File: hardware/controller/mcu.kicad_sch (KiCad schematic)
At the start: 21 parts, among them J12 USB_C_Receptacle_USB2.0_14P, J5 Screw_Terminal_01x02, J6 Screw_Terminal_01x02, U1 ESP32-C3-MINI-1, U6 TPS1H200AQDGNRQ1

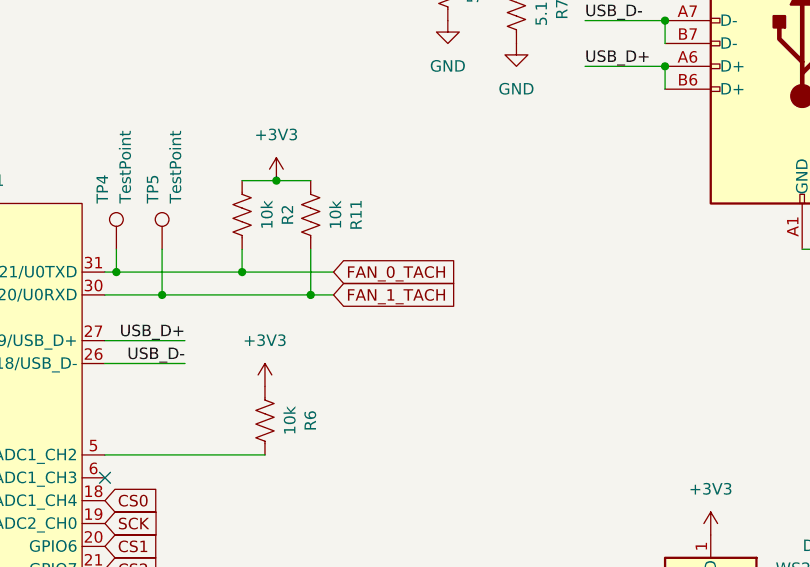
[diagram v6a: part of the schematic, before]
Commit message: Rounded corners, fixed up labels
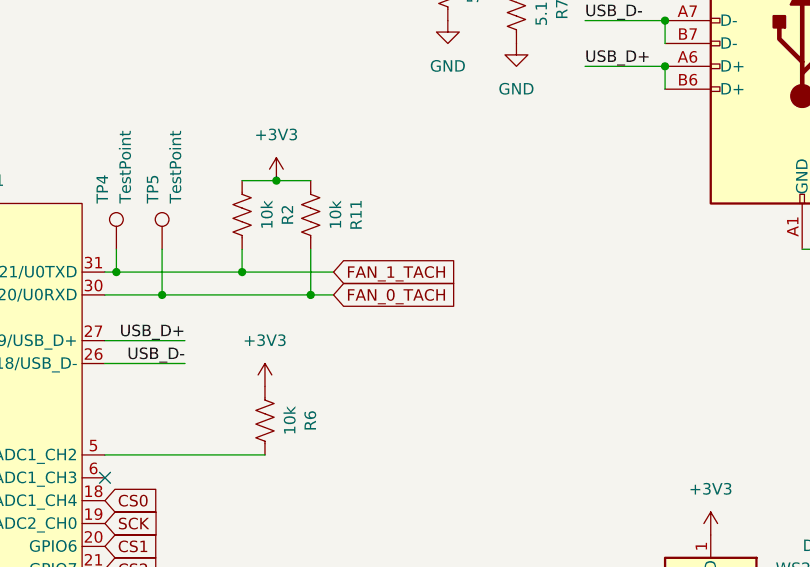
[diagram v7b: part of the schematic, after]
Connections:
- net FAN_0_TACH: now also R11.1, TP5.1, U1.30 (GPIO20/U0RXD); no longer R2.1, TP4.1, U1.31 (GPIO21/U0TXD)
- net FAN_1_TACH: now also R2.1, TP4.1, U1.31 (GPIO21/U0TXD); no longer R11.1, TP5.1, U1.30 (GPIO20/U0RXD)
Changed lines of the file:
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@@
 	(global_label "FAN_1_TACH"
 		(shape input)
-		(at 199.39 77.47 0)
+		(at 199.39 74.93 0)
 		(fields_autoplaced yes)
 		(effects
@@
 		)
 		(property "Intersheetrefs" "${INTERSHEET_REFS}"
-			(at 213.6843 77.47 0)
+			(at 213.6843 74.93 0)
 			(effects
 				(font
@@
 	(global_label "FAN_0_TACH"
 		(shape input)
-		(at 199.39 74.93 0)
+		(at 199.39 77.47 0)
 		(fields_autoplaced yes)
 		(effects
@@
 		)
 		(property "Intersheetrefs" "${INTERSHEET_REFS}"
-			(at 213.6843 74.93 0)
+			(at 213.6843 77.47 0)
 			(effects
 				(font

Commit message: Add LCSC numbers
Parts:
- C1: LCSC (none) -> C49678
- C12, C8: LCSC (none) -> C28323
- C7: LCSC` (none) -> C15850
- D1: LCSC (none) -> C114586
- D2: LCSC (none) -> C84256
- J12: LCSC (none) -> C2765186
- R1, R7: LCSC (none) -> C27834
- R11, R2, R5, R6: LCSC (none) -> C84376
- R3: LCSC (none) -> C2828857
- U1: LCSC (none) -> C2934569
- U6: LCSC (none) -> C2653785
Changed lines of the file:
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@@
+			)
+		)
+		(property "LCSC" "C84376"
+			(at 196.85 68.58 90)
+			(effects
+				(font
+					(size 1.27 1.27)
+				)
+				(hide yes)
 			)
 		)
@@
 			)
 		)
+		(property "LCSC" "C27834"
+			(at 219.71 45.72 90)
+			(effects
+				(font
+					(size 1.27 1.27)
+				)
+				(hide yes)
+			)
+		)
 		(pin "1"
 		)
@@
 		)
 		(property "Description" "Unpolarized capacitor"
+			(at 99.06 74.93 0)
+			(effects
+				(font
+					(size 1.27 1.27)
+				)
+				(hide yes)
+			)
+		)
+		(property "LCSC`" "C15850"
 			(at 99.06 74.93 0)
 			(effects
@@
 			)
 		)
+		(property "LCSC" "C2828857"
+			(at 64.77 100.33 0)
+			(effects
+				(font
+					(size 1.27 1.27)
+				)
+				(hide yes)
+			)
+		)
 		(pin "1"
 		)
@@
 			)
 		)
+		(property "LCSC" "C2765186"
+			(at 251.46 49.53 0)
+			(effects
+				(font
+					(size 1.27 1.27)
+				)
+				(hide yes)
+			)
+		)
+		(property "Field6" ""
+			(at 251.46 49.53 0)
+			(effects
+				(font
+					(size 1.27 1.27)
+				)
+				(hide yes)
+			)
+		)
 		(pin "A1"
 		)
@@
 			)
 		)
+		(property "LCSC" "C84376"
+			(at 189.23 68.58 90)
+			(effects
+				(font
+					(size 1.27 1.27)
+				)
+				(hide yes)
+			)
+		)
 		(pin "1"
 		)
@@
 		(property "Description" "Resistor, US symbol"
 			(at 212.09 43.18 0)
+			(effects
+				(font
+					(size 1.27 1.27)
+				)
+				(hide yes)
+			)
+		)
+		(property "LCSC" "C27834"
+			(at 212.09 43.18 90)
 			(effects
 				(font
@@
 			)
 		)
+		(property "LCSC" "C2934569"
+			(at 146.05 92.71 0)
+			(effects
+				(font
+					(size 1.27 1.27)
+				)
+				(hide yes)
+			)
+		)
 		(pin "11"
 		)
@@
 			)
 		)
+		(property "LCSC" "C84256"
+			(at 64.77 92.71 90)
+			(effects
+				(font
+					(size 1.27 1.27)
+				)
+				(hide yes)
+			)
+		)
 		(pin "2"
 		)
@@
 			)
 		)
+		(property "LCSC" "C49678"
+			(at 113.03 139.7 0)
+			(effects
+				(font
+					(size 1.27 1.27)
+				)
+				(hide yes)
+			)
+		)
+		(property "Field6" ""
+			(at 113.03 139.7 0)
+			(effects
+				(font
+					(size 1.27 1.27)
+				)
+				(hide yes)
+			)
+		)
 		(pin "2"
 		)
@@
 			)
 		)
+		(property "LCSC" "C84376"
+			(at 99.06 64.77 90)
+			(effects
+				(font
+					(size 1.27 1.27)
+				)
+				(hide yes)
+			)
+		)
 		(pin "1"
 		)
@@
 			)
 		)
+		(property "LCSC" "C84376"
+			(at 191.77 91.44 90)
+			(effects
+				(font
+					(size 1.27 1.27)
+				)
+				(hide yes)
+			)
+		)
+		(property "Field6" ""
+			(at 191.77 91.44 90)
+			(effects
+				(font
+					(size 1.27 1.27)
+				)
+				(hide yes)
+			)
+		)
 		(pin "1"
 		)
@@
 			)
 		)
+		(property "LCSC" "C28323"
+			(at 135.89 52.07 0)
+			(effects
+				(font
+					(size 1.27 1.27)
+				)
+				(hide yes)
+			)
+		)
 		(pin "2"
 		)
@@
 			)
 		)
+		(property "LCSC" "C2653785"
+			(at 80.01 142.24 0)
+			(effects
+				(font
+					(size 1.27 1.27)
+				)
+				(hide yes)
+			)
+		)
 		(pin "4"
 		)
@@
 			)
 		)
+		(property "LCSC" "C28323"
+			(at 262.89 111.76 0)
+			(effects
+				(font
+					(size 1.27 1.27)
+				)
+				(hide yes)
+			)
+		)
 		(pin "2"
 		)
@@
 			(at 241.3 111.76 0)
 			(effects
+				(font
+					(size 1.27 1.27)
+				)
+				(hide yes)
+			)
+		)
+		(property "LCSC" "C114586"
+			(at 241.3 111.76 0)
+			(effects
